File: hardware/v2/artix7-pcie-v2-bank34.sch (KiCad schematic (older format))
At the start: 6 parts, among them J1 Conn_02x20_Odd_Even, U1 XC7A75T-FGG484

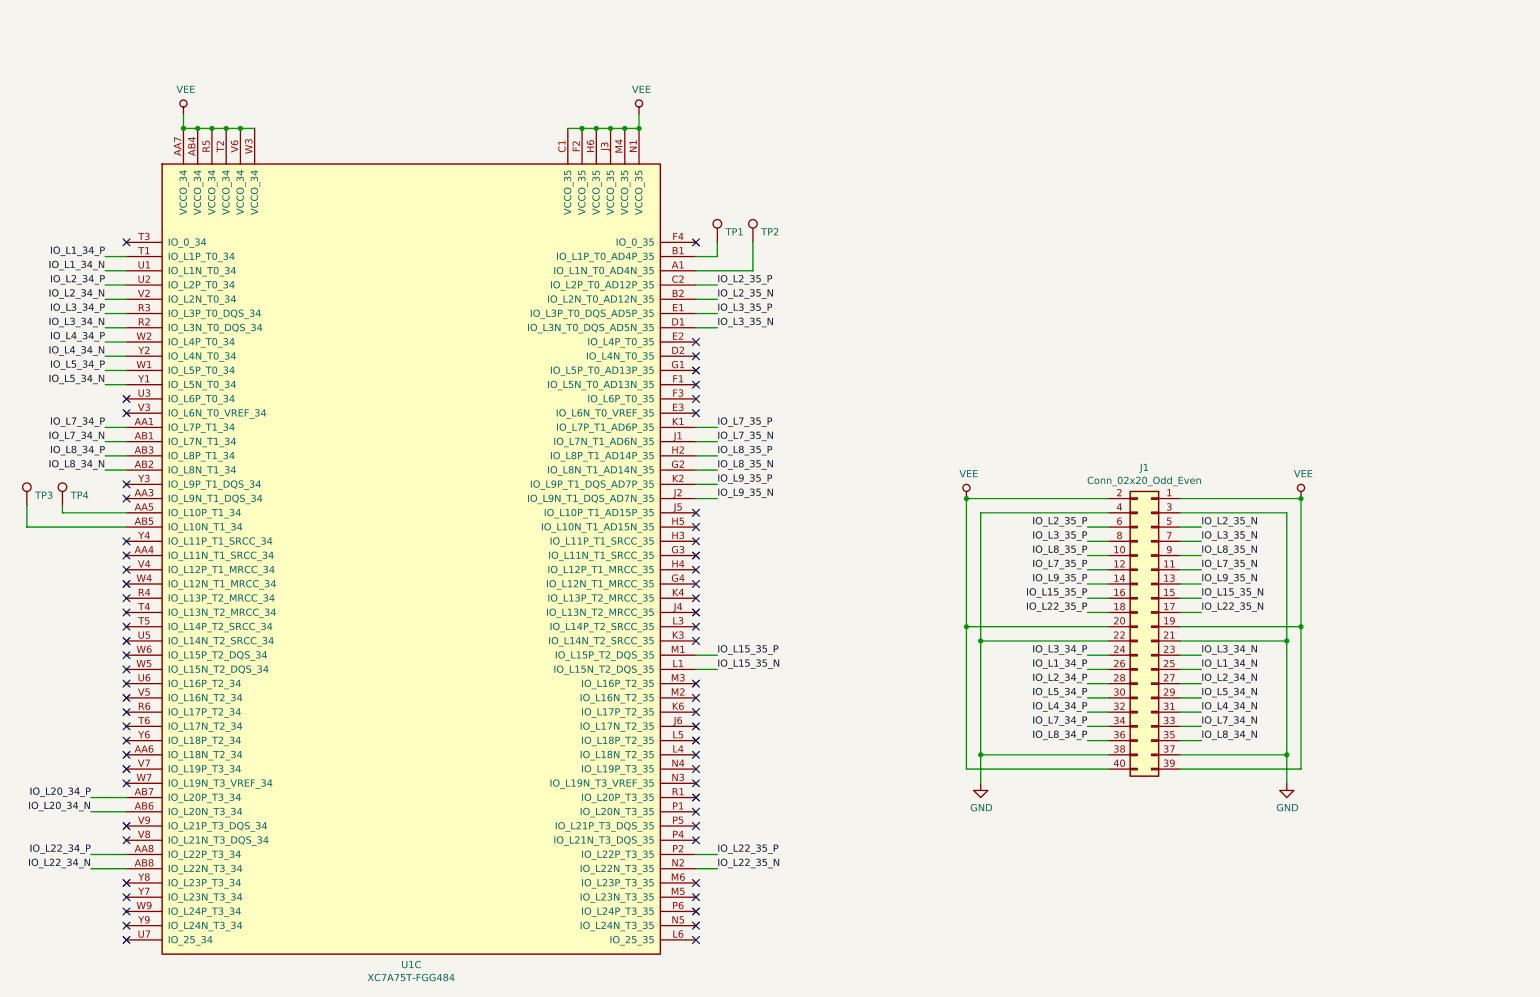
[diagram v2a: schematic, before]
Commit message: v2 pcb/schematic update : drc passing, need to add caps
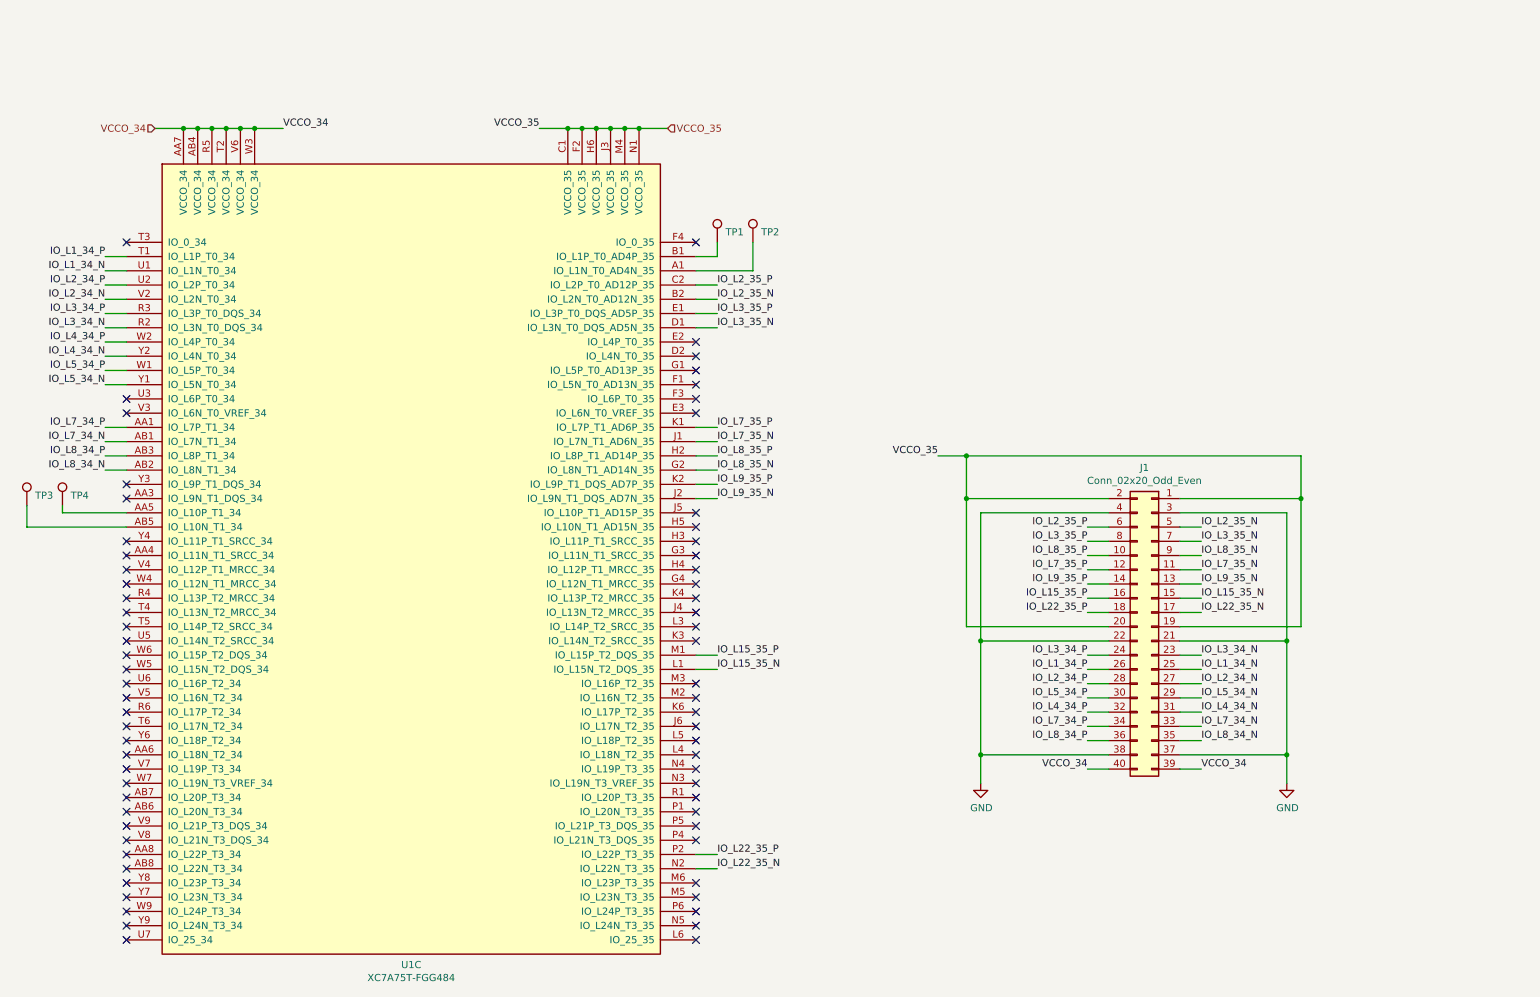
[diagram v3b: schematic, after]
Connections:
- net IO_L20_34_N: no longer names the net of U1.AB6 (IO_L20N_T3_34)
- net IO_L20_34_P: no longer names the net of U1.AB7 (IO_L20P_T3_34)
- net IO_L22_34_N: no longer names the net of U1.AB8 (IO_L22N_T3_34)
- net IO_L22_34_P: no longer names the net of U1.AA8 (IO_L22P_T3_34)
- net VEE renamed VCCO_35
- net VCCO_35: no longer J1.39 (Pin_39), J1.40 (Pin_40), U1.AA7 (VCCO_34), U1.AB4 (VCCO_34), U1.R5 (VCCO_34), U1.T2 (VCCO_34), U1.V6 (VCCO_34), U1.W3 (VCCO_34)
- new net VCCO_34: J1.39 (Pin_39), J1.40 (Pin_40), U1.AA7 (VCCO_34), U1.AB4 (VCCO_34), U1.R5 (VCCO_34), U1.T2 (VCCO_34), U1.V6 (VCCO_34), U1.W3 (VCCO_34)
- no-connect marks 64 -> 68
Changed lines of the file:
@@
 EESchema Schematic File Version 4
-LIBS:artix7-pcie-v2-cache
 EELAYER 30 0
 EELAYER END
 $Descr A4 11693 8268
 encoding utf-8
-Sheet 6 7
+Sheet 7 7
 Title ""
 Date ""
@@
 Comment4 ""
 $EndDescr
-$Comp
-L artix7-pcie-v2:XC7A75T-FGG484 U1
-U 3 1 5E6D68C3
-P 3300 4150
-F 0 "U1" H 3300 1175 50  0000 C CNN
-F 1 "XC7A75T-FGG484" H 3300 1084 50  0000 C CNN
-F 2 "artix7-pcie-v2:Xilinx_FGG484" H 3300 4150 50  0001 C CNN
-F 3 "" H 3300 4150 50  0000 C CNN
-	3    3300 4150
-	1    0    0    -1
-$EndComp
 $Comp
 L tom-connectors:Conn_02x20_Odd_Even J?
@@
 Wire Wire Line
 	7200 4750 7200 3850
-Wire Wire Line
-	8700 5750 9550 5750
-Wire Wire Line
-	9550 5750 9550 4750
-Connection ~ 9550 4750
-Wire Wire Line
-	8200 5750 7200 5750
-Wire Wire Line
-	7200 5750 7200 4750
-Connection ~ 7200 4750
 $Comp
 L power:GND #PWR?
@@
 Wire Wire Line
 	7300 4850 7300 3950
-Wire Wire Line
-	1050 5950 1300 5950
-Wire Wire Line
-	1050 6050 1300 6050
-Wire Wire Line
-	1050 6350 1300 6350
-Wire Wire Line
-	1050 6450 1300 6450
 $Bitmap
 Pos 9350 2050
@@
 Text Label 1150 3650 2    50   ~ 0
 IO_L8_34_N
-Text Label 1050 5950 2    50   ~ 0
-IO_L20_34_P
-Text Label 1050 6050 2    50   ~ 0
-IO_L20_34_N
-Text Label 1050 6350 2    50   ~ 0
-IO_L22_34_P
-Text Label 1050 6450 2    50   ~ 0
-IO_L22_34_N
 Text Label 5450 2350 0    50   ~ 0
 IO_L2_35_P
@@
 NoConn ~ 1300 3150
 NoConn ~ 1300 2050
-Wire Wire Line
-	4400 1250 4500 1250
-Connection ~ 4500 1250
-Wire Wire Line
-	4500 1250 4600 1250
-Connection ~ 4600 1250
-Wire Wire Line
-	4600 1250 4700 1250
-Connection ~ 4700 1250
-Wire Wire Line
-	4700 1250 4800 1250
-Connection ~ 4800 1250
-Wire Wire Line
-	4800 1250 4900 1250
-Wire Wire Line
-	4900 1250 4900 1150
-Connection ~ 4900 1250
-Wire Wire Line
-	2200 1250 2100 1250
-Connection ~ 1800 1250
-Wire Wire Line
-	1800 1250 1700 1250
-Connection ~ 1900 1250
-Wire Wire Line
-	1900 1250 1800 1250
-Connection ~ 2000 1250
-Wire Wire Line
-	2000 1250 1900 1250
-Connection ~ 2100 1250
-Wire Wire Line
-	2100 1250 2000 1250
-Wire Wire Line
-	1700 1250 1700 1150
-Connection ~ 1700 1250
 NoConn ~ 5300 2050
 $Comp
@@
 	1    0    0    -1
 $EndComp
-$Comp
-L power:VEE #PWR0126
-U 1 1 5F4DD67C
-P 1700 1150
-F 0 "#PWR0126" H 1700 1000 50  0001 C CNN
-F 1 "VEE" H 1717 1323 50  0000 C CNN
-F 2 "" H 1700 1150 50  0001 C CNN
-F 3 "" H 1700 1150 50  0001 C CNN
-	1    1700 1150
-	1    0    0    -1
-$EndComp
-$Comp
-L power:VEE #PWR0127
-U 1 1 5F4E04F5
-P 4900 1150
-F 0 "#PWR0127" H 4900 1000 50  0001 C CNN
-F 1 "VEE" H 4917 1323 50  0000 C CNN
-F 2 "" H 4900 1150 50  0001 C CNN
-F 3 "" H 4900 1150 50  0001 C CNN
-	1    4900 1150
-	1    0    0    -1
-$EndComp
-$Comp
-L power:VEE #PWR0128
-U 1 1 5F4E5BA1
-P 9550 3850
-F 0 "#PWR0128" H 9550 3700 50  0001 C CNN
-F 1 "VEE" H 9567 4023 50  0000 C CNN
-F 2 "" H 9550 3850 50  0001 C CNN
-F 3 "" H 9550 3850 50  0001 C CNN
-	1    9550 3850
-	1    0    0    -1
-$EndComp
-Connection ~ 9550 3850
-$Comp
-L power:VEE #PWR0129
-U 1 1 5F4E5DA1
-P 7200 3850
-F 0 "#PWR0129" H 7200 3700 50  0001 C CNN
-F 1 "VEE" H 7217 4023 50  0000 C CNN
-F 2 "" H 7200 3850 50  0001 C CNN
-F 3 "" H 7200 3850 50  0001 C CNN
-	1    7200 3850
-	1    0    0    -1
-$EndComp
-Connection ~ 7200 3850
 Wire Wire Line
 	1300 2550 1150 2550
@@
 Text Label 8850 4950 0    50   ~ 0
 IO_L3_34_N
+Wire Wire Line
+	9550 3850 9550 3550
+Wire Wire Line
+	9550 3550 7200 3550
+Connection ~ 9550 3850
+Wire Wire Line
+	7200 3850 7200 3550
+Connection ~ 7200 3850
+Connection ~ 7200 3550
+Wire Wire Line
+	7200 3550 7000 3550
+NoConn ~ 1300 5950
+NoConn ~ 1300 6050
+NoConn ~ 1300 6350
+NoConn ~ 1300 6450
+Connection ~ 2200 1250
+Wire Wire Line
+	2200 1250 2100 1250
+Connection ~ 2100 1250
+Wire Wire Line
+	2100 1250 2000 1250
+Connection ~ 2000 1250
+Wire Wire Line
+	2000 1250 1900 1250
+Connection ~ 1900 1250
+Wire Wire Line
+	4800 1250 4900 1250
+Connection ~ 4800 1250
+Wire Wire Line
+	4700 1250 4800 1250
+Connection ~ 4700 1250
+Wire Wire Line
+	4600 1250 4700 1250
+Connection ~ 4600 1250
+Wire Wire Line
+	4500 1250 4600 1250
+Connection ~ 4500 1250
+Wire Wire Line
+	4400 1250 4500 1250
+Connection ~ 4400 1250
+Wire Wire Line
+	1900 1250 1800 1250
+Connection ~ 1800 1250
+Wire Wire Line
+	1700 1250 1500 1250
+Wire Wire Line
+	1800 1250 1700 1250
+Connection ~ 1700 1250
+$Comp
+L artix7-pcie-v2:XC7A75T-FGG484 U1
+U 3 1 5E6D68C3
+P 3300 4150
+F 0 "U1" H 3300 1175 50  0000 C CNN
+F 1 "XC7A75T-FGG484" H 3300 1084 50  0000 C CNN
+F 2 "artix7-pcie-v2:Xilinx_FGG484" H 3300 4150 50  0001 C CNN
+F 3 "" H 3300 4150 50  0000 C CNN
+	3    3300 4150
+	1    0    0    -1
+$EndComp
+Text Label 7000 3550 2    50   ~ 0
+VCCO_35
+Wire Wire Line
+	8050 5750 8200 5750
+Wire Wire Line
+	8700 5750 8850 5750
+Text Label 8850 5750 0    50   ~ 0
+VCCO_34
+Text Label 8050 5750 2    50   ~ 0
+VCCO_34
+Text Label 4200 1250 2    50   ~ 0
+VCCO_35
+Text HLabel 5100 1250 2    50   Input ~ 0
+VCCO_35
+Connection ~ 4900 1250
+Wire Wire Line
+	5100 1250 4900 1250
+Wire Wire Line
+	4400 1250 4200 1250
+Wire Wire Line
+	2200 1250 2400 1250
+Text Label 2400 1250 0    50   ~ 0
+VCCO_34
+Text HLabel 1500 1250 0    50   Input ~ 0
+VCCO_34
 $EndSCHEMATC

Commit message: v2 hardware: pcb progress commit, 155 unrouted
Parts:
- added C18, C23, C85, C86: 100uF/6.3V/X5R, tom-passives:C_1206_3216Metric, symbol tom-passives:C
- added C87, C88, C89, C90: 4.7uF/6.3V/X5R, tom-passives:C_0402_1005Metric, symbol tom-passives:C
- added C91, C92, C93, C94, C95, C96, C97, C98: 0.47uF/6.3V/X5R, tom-passives:C_0402_1005Metric, symbol tom-passives:C
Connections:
- net GND: now also C18.2, C23.2, C85.2, C86.2, C87.2, C88.2, C89.2, C90.2, C91.2, C92.2, C93.2, C94.2, C95.2, C96.2, C97.2, C98.2
- net VCCO_34: now also C18.1, C85.1, C87.1, C89.1, C91.1, C93.1, C95.1, C97.1
- net VCCO_35: now also C23.1, C86.1, C88.1, C90.1, C92.1, C94.1, C96.1, C98.1
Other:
- note added: "ULX3S"

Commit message: v2 schematic/pcb progress commit - 12 unrouted
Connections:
- net IO_L7_35_N: now also J1.13 (Pin_13); no longer J1.11 (Pin_11)
- net IO_L7_35_P: now also J1.14 (Pin_14); no longer J1.12 (Pin_12)
- net IO_L9_35_N: now also J1.11 (Pin_11); no longer J1.13 (Pin_13)
- net IO_L9_35_P: now also J1.12 (Pin_12); no longer J1.14 (Pin_14)
- net at TP2.1: now also U1.B2 (IO_L2N_T0_AD12N_35); no longer U1.A1 (IO_L1N_T0_AD4N_35)
- net at TP1.1: now also U1.C2 (IO_L2P_T0_AD12P_35); no longer U1.B1 (IO_L1P_T0_AD4P_35)
- net IO_L5_35_N: now reaches U1.F1 (IO_L5N_T0_AD13N_35)
- net IO_L5_35_N: now also J1.9 (Pin_9)
- net IO_L5_35_P: now reaches U1.G1 (IO_L5P_T0_AD13P_35)
- net IO_L5_35_P: now also J1.10 (Pin_10)
- net IO_L2_35_N renamed IO_L1_35_N
- net IO_L1_35_N: now also U1.A1 (IO_L1N_T0_AD4N_35); no longer U1.B2 (IO_L2N_T0_AD12N_35)
- net IO_L2_35_P renamed IO_L1_35_P
- net IO_L1_35_P: now also U1.B1 (IO_L1P_T0_AD4P_35); no longer U1.C2 (IO_L2P_T0_AD12P_35)
- net IO_L8_35_N: no longer names the net of U1.G2 (IO_L8N_T1_AD14N_35)
- net IO_L8_35_N: no longer J1.9 (Pin_9)
- net IO_L8_35_P: no longer names the net of U1.H2 (IO_L8P_T1_AD14P_35)
- net IO_L8_35_P: no longer J1.10 (Pin_10)
- no-connect marks 68 -> 66
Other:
- moved on the sheet: TP1, TP2
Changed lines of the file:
@@
 	1150 3450 1300 3450
-Wire Wire Line
-	5450 2350 5300 2350
-Wire Wire Line
-	5450 2450 5300 2450
 Wire Wire Line
 	5450 6450 5300 6450
@@
 Text Label 1150 3650 2    50   ~ 0
 IO_L8_34_N
-Text Label 5450 2350 0    50   ~ 0
-IO_L2_35_P
-Text Label 5450 2450 0    50   ~ 0
-IO_L2_35_N
+Text Label 5450 2150 0    50   ~ 0
+IO_L1_35_P
+Text Label 5450 2250 0    50   ~ 0
+IO_L1_35_N
 Text Label 5450 2550 0    50   ~ 0
 IO_L3_35_P
@@
 Text Label 5450 3450 0    50   ~ 0
 IO_L7_35_N
-Text Label 5450 3550 0    50   ~ 0
-IO_L8_35_P
-Text Label 5450 3650 0    50   ~ 0
-IO_L8_35_N
+Text Label 5450 2950 0    50   ~ 0
+IO_L5_35_P
+Text Label 5450 3050 0    50   ~ 0
+IO_L5_35_N
 Text Label 5450 3750 0    50   ~ 0
 IO_L9_35_P
@@
 IO_L22_35_N
 Text Label 8050 4050 2    50   ~ 0
-IO_L2_35_P
+IO_L1_35_P
 Text Label 8050 4150 2    50   ~ 0
 IO_L3_35_P
 Text Label 8050 4250 2    50   ~ 0
-IO_L8_35_P
+IO_L5_35_P
+Text Label 8050 4450 2    50   ~ 0
+IO_L7_35_P
 Text Label 8050 4350 2    50   ~ 0
-IO_L7_35_P
-Text Label 8050 4450 2    50   ~ 0
 IO_L9_35_P
 Text Label 8050 4550 2    50   ~ 0
@@
 IO_L8_34_P
 Text Label 8850 4050 0    50   ~ 0
-IO_L2_35_N
+IO_L1_35_N
 Text Label 8850 4150 0    50   ~ 0
 IO_L3_35_N
 Text Label 8850 4250 0    50   ~ 0
-IO_L8_35_N
+IO_L5_35_N
+Text Label 8850 4450 0    50   ~ 0
+IO_L7_35_N
 Text Label 8850 4350 0    50   ~ 0
-IO_L7_35_N
-Text Label 8850 4450 0    50   ~ 0
 IO_L9_35_N
 Text Label 8850 4550 0    50   ~ 0
@@
 NoConn ~ 5300 2750
 NoConn ~ 5300 2850
-NoConn ~ 5300 2950
-NoConn ~ 5300 3050
 NoConn ~ 5300 3150
 NoConn ~ 5300 3250
@@
 L tom-mechanical:TestPoint TP1
 U 1 1 5F37E446
-P 5450 2050
-F 0 "TP1" H 5508 2122 50  0000 L CNN
-F 1 "TestPoint" H 5508 2077 50  0001 L CNN
-F 2 "tom-mechanical:TestPoint_Pad_D1.5mm" H 5650 2050 50  0001 C CNN
-F 3 "~" H 5650 2050 50  0001 C CNN
-	1    5450 2050
-	1    0    0    -1
+P 6050 2350
+F 0 "TP1" H 6108 2422 50  0000 L CNN
+F 1 "TestPoint" H 6108 2377 50  0001 L CNN
+F 2 "tom-mechanical:TestPoint_Pad_D1.5mm" H 6250 2350 50  0001 C CNN
+F 3 "~" H 6250 2350 50  0001 C CNN
+	1    6050 2350
+	0    1    -1   0
 $EndComp
 $Comp
 L tom-mechanical:TestPoint TP2
 U 1 1 5F37EBC2
-P 5700 2050
-F 0 "TP2" H 5758 2122 50  0000 L CNN
-F 1 "TestPoint" H 5758 2077 50  0001 L CNN
-F 2 "tom-mechanical:TestPoint_Pad_D1.5mm" H 5900 2050 50  0001 C CNN
-F 3 "~" H 5900 2050 50  0001 C CNN
-	1    5700 2050
-	1    0    0    -1
-$EndComp
-Wire Wire Line
-	5450 2050 5450 2150
-Wire Wire Line
-	5450 2150 5300 2150
-Wire Wire Line
-	5300 2250 5700 2250
-Wire Wire Line
-	5700 2250 5700 2050
+P 6050 2450
+F 0 "TP2" H 6108 2522 50  0000 L CNN
+F 1 "TestPoint" H 6108 2477 50  0001 L CNN
+F 2 "tom-mechanical:TestPoint_Pad_D1.5mm" H 6250 2450 50  0001 C CNN
+F 3 "~" H 6250 2450 50  0001 C CNN
+	1    6050 2450
+	0    1    1    0
+$EndComp
 $Comp
 L tom-mechanical:TestPoint TP4
@@
 	8200 5750 8050 5750
 Connection ~ 8200 5750
+Wire Wire Line
+	5300 2350 6050 2350
+Wire Wire Line
+	5300 2450 6050 2450
+Wire Wire Line
+	5300 2250 5450 2250
+Wire Wire Line
+	5450 2150 5300 2150
+Wire Wire Line
+	5300 2950 5450 2950
+Wire Wire Line
+	5300 3050 5450 3050
 $EndSCHEMATC

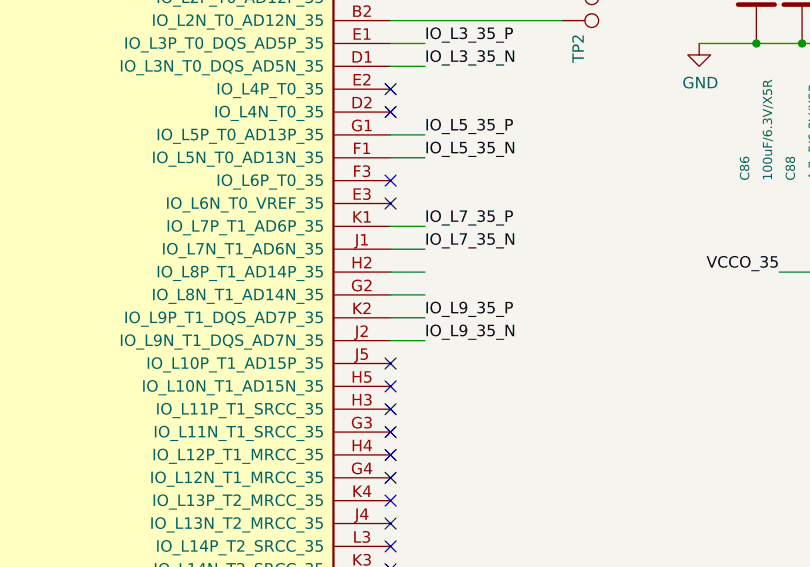
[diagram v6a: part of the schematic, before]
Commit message: v2 hardware: all tracks routed, erc/drc pass
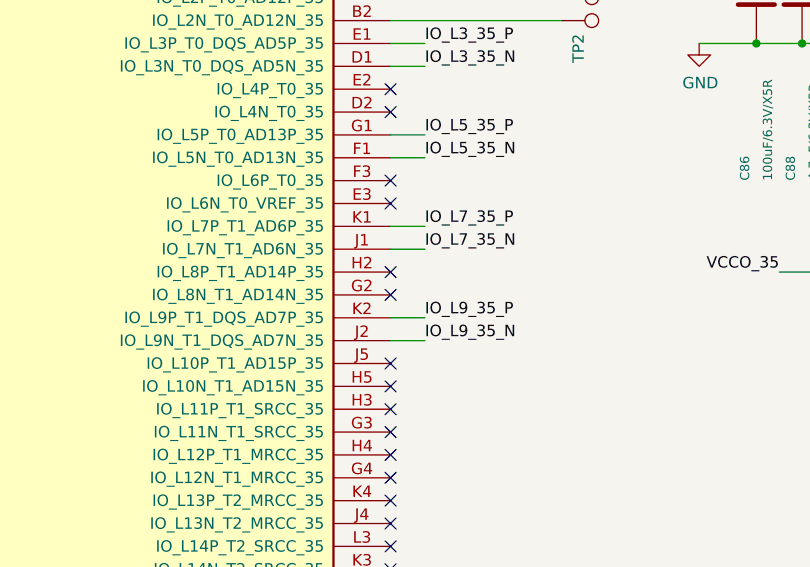
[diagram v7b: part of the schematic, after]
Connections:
- no-connect marks 66 -> 68
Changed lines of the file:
@@
 	5300 3750 5450 3750
-Wire Wire Line
-	5450 3650 5300 3650
-Wire Wire Line
-	5300 3550 5450 3550
 Wire Wire Line
 	5450 3450 5300 3450
@@
 Wire Wire Line
 	5300 3050 5450 3050
+NoConn ~ 5300 3550
+NoConn ~ 5300 3650
 $EndSCHEMATC

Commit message: v2 hardware: add Digikey part numbers to schematic and generate bom
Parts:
- C18, C23, C85, C86: Vendor (none) -> 478-12404-1-ND
- C87, C88, C89, C90: Vendor (none) -> 490-5915-1-ND
- C91, C92, C93, C94, C95, C96, C97, C98: Vendor (none) -> 1276-CL05Y474KP5VPNCCT-ND
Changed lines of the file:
@@
 F 2 "tom-passives:C_1206_3216Metric" H 6938 1050 30  0001 C CNN
 F 3 "" H 6900 1200 60  0001 C CNN
+F 4 "478-12404-1-ND" H 6900 1200 50  0001 C CNN "Vendor"
 	1    6900 1200
 	1    0    0    -1
@@
 F 2 "tom-passives:C_0402_1005Metric" H 7138 1050 30  0001 C CNN
 F 3 "" H 7100 1200 60  0001 C CNN
+F 4 "490-5915-1-ND" H 7100 1200 50  0001 C CNN "Vendor"
 	1    7100 1200
 	1    0    0    -1
@@
 F 2 "tom-passives:C_0402_1005Metric" H 7338 1050 30  0001 C CNN
 F 3 "" H 7300 1200 60  0001 C CNN
+F 4 "490-5915-1-ND" H 7300 1200 50  0001 C CNN "Vendor"
 	1    7300 1200
 	1    0    0    -1
@@
 F 2 "tom-passives:C_0402_1005Metric" H 7538 1050 30  0001 C CNN
 F 3 "" H 7500 1200 60  0001 C CNN
+F 4 "1276-CL05Y474KP5VPNCCT-ND" H 7500 1200 50  0001 C CNN "Vendor"
 	1    7500 1200
 	1    0    0    -1
@@
 F 2 "tom-passives:C_0402_1005Metric" H 7738 1050 30  0001 C CNN
 F 3 "" H 7700 1200 60  0001 C CNN
+F 4 "1276-CL05Y474KP5VPNCCT-ND" H 7700 1200 50  0001 C CNN "Vendor"
 	1    7700 1200
 	1    0    0    -1
@@
 F 2 "tom-passives:C_0402_1005Metric" H 7938 1050 30  0001 C CNN
 F 3 "" H 7900 1200 60  0001 C CNN
+F 4 "1276-CL05Y474KP5VPNCCT-ND" H 7900 1200 50  0001 C CNN "Vendor"
 	1    7900 1200
 	1    0    0    -1
@@
 F 2 "tom-passives:C_0402_1005Metric" H 8138 1050 30  0001 C CNN
 F 3 "" H 8100 1200 60  0001 C CNN
+F 4 "1276-CL05Y474KP5VPNCCT-ND" H 8100 1200 50  0001 C CNN "Vendor"
 	1    8100 1200
 	1    0    0    -1
@@
 F 2 "tom-passives:C_1206_3216Metric" H 6938 2200 30  0001 C CNN
 F 3 "" H 6900 2350 60  0001 C CNN
+F 4 "478-12404-1-ND" H 6900 2350 50  0001 C CNN "Vendor"
 	1    6900 2350
 	1    0    0    -1
@@
 F 2 "tom-passives:C_0402_1005Metric" H 7138 2200 30  0001 C CNN
 F 3 "" H 7100 2350 60  0001 C CNN
+F 4 "490-5915-1-ND" H 7100 2350 50  0001 C CNN "Vendor"
 	1    7100 2350
 	1    0    0    -1
@@
 F 2 "tom-passives:C_0402_1005Metric" H 7338 2200 30  0001 C CNN
 F 3 "" H 7300 2350 60  0001 C CNN
+F 4 "490-5915-1-ND" H 7300 2350 50  0001 C CNN "Vendor"
 	1    7300 2350
 	1    0    0    -1
@@
 F 2 "tom-passives:C_0402_1005Metric" H 7538 2200 30  0001 C CNN
 F 3 "" H 7500 2350 60  0001 C CNN
+F 4 "1276-CL05Y474KP5VPNCCT-ND" H 7500 2350 50  0001 C CNN "Vendor"
 	1    7500 2350
 	1    0    0    -1
@@
 F 2 "tom-passives:C_0402_1005Metric" H 7738 2200 30  0001 C CNN
 F 3 "" H 7700 2350 60  0001 C CNN
+F 4 "1276-CL05Y474KP5VPNCCT-ND" H 7700 2350 50  0001 C CNN "Vendor"
 	1    7700 2350
 	1    0    0    -1
@@
 F 2 "tom-passives:C_0402_1005Metric" H 7938 2200 30  0001 C CNN
 F 3 "" H 7900 2350 60  0001 C CNN
+F 4 "1276-CL05Y474KP5VPNCCT-ND" H 7900 2350 50  0001 C CNN "Vendor"
 	1    7900 2350
 	1    0    0    -1
@@
 F 2 "tom-passives:C_0402_1005Metric" H 8138 2200 30  0001 C CNN
 F 3 "" H 8100 2350 60  0001 C CNN
+F 4 "1276-CL05Y474KP5VPNCCT-ND" H 8100 2350 50  0001 C CNN "Vendor"
 	1    8100 2350
 	1    0    0    -1
@@
 F 2 "tom-passives:C_1206_3216Metric" H 9788 3600 30  0001 C CNN
 F 3 "" H 9750 3750 60  0001 C CNN
+F 4 "478-12404-1-ND" H 9750 3750 50  0001 C CNN "Vendor"
 	1    9750 3750
 	1    0    0    -1
@@
 F 2 "tom-passives:C_1206_3216Metric" H 8238 5800 30  0001 C CNN
 F 3 "" H 8200 5950 60  0001 C CNN
+F 4 "478-12404-1-ND" H 8200 5950 50  0001 C CNN "Vendor"
 	1    8200 5950
 	1    0    0    -1
